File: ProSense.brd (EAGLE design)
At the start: 16.3 x 37.7 mm, 25 parts

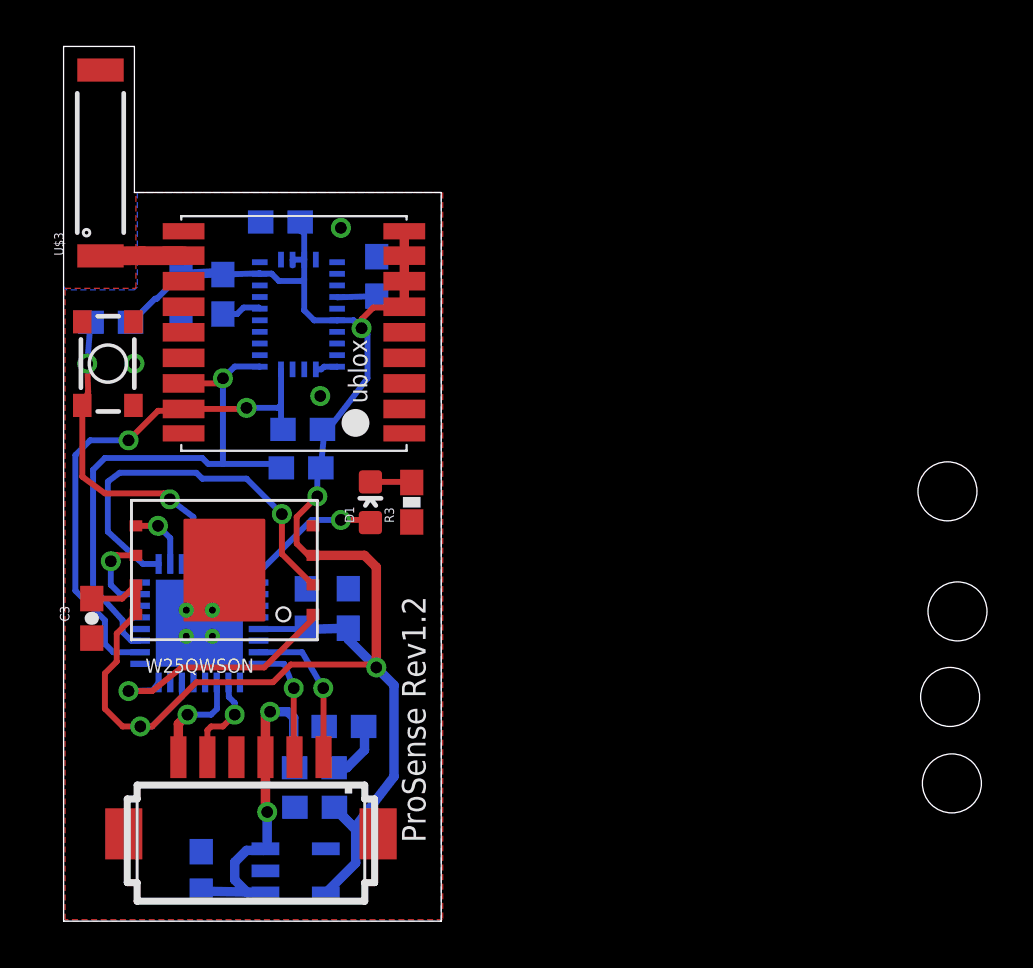
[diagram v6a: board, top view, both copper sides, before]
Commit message: Fixed up a few things. Need to fix ground pads and holes for qfn
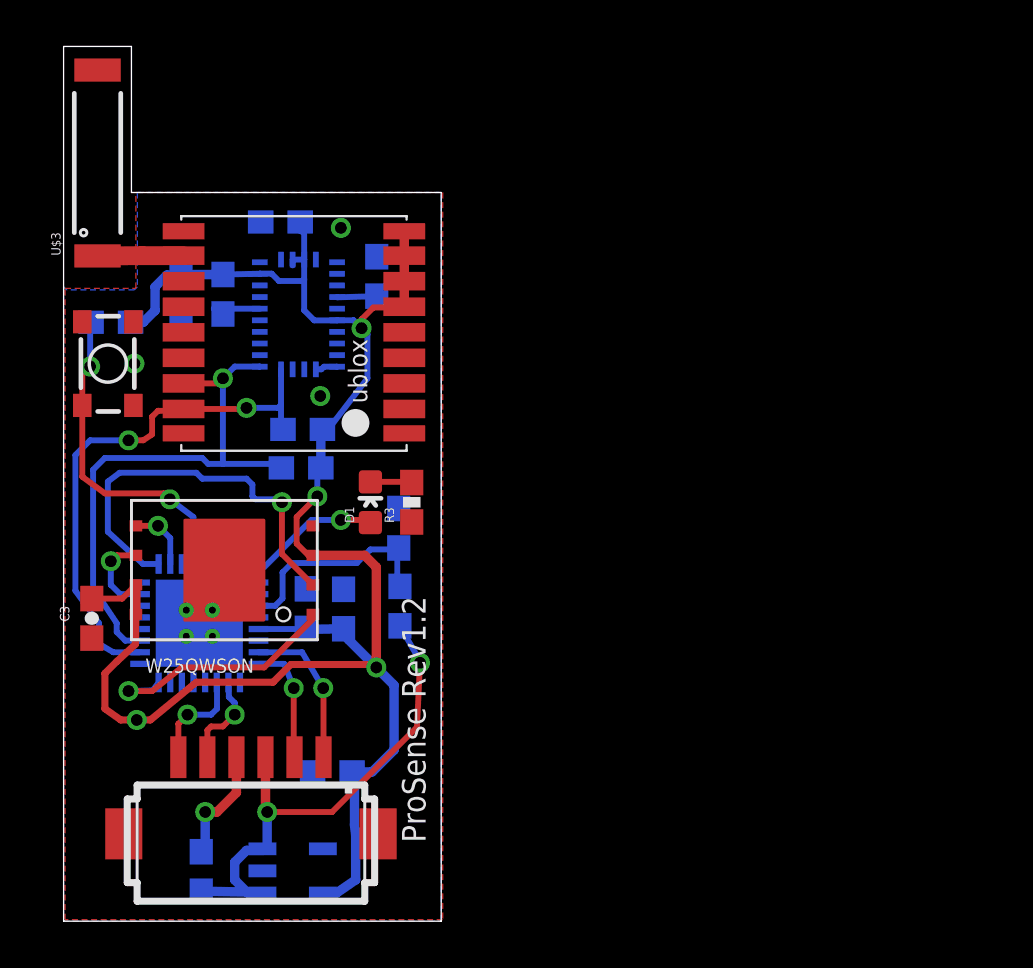
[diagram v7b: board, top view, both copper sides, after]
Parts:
- removed FRAME1: FRAME-LEDGER, SparkFun-Aesthetics:CREATIVE_COMMONS
- moved R2 8.86 mm to (20.0, 21.2), turned to 270 degrees
- moved R1 7.87 mm to (20.1, 17.9), turned to 270 degrees
- moved C15 1.70 mm to (17.2, 10.7)
- moved C7 0.20 mm to (17.6, 17.8)
- moved U$3 0.13 mm to (7.05, 37.0)
- moved MIC5205 0.13 mm to (15.4, 6.48)
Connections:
- net BAT_MONITOR: now also MCU.27; no longer MCU.24
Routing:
- net VIN: track 16.0 -> 23.3 mm
- net BAT_MONITOR: track 2.65 -> 9.36 mm
- net GND: track 2.69 -> 8.63 mm, vias 3 -> 4
- net VCC: track 84.4 -> 83.4 mm
- net WS_DO: track 16.8 -> 17.4 mm
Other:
- outline, holes or cut-outs redrawn

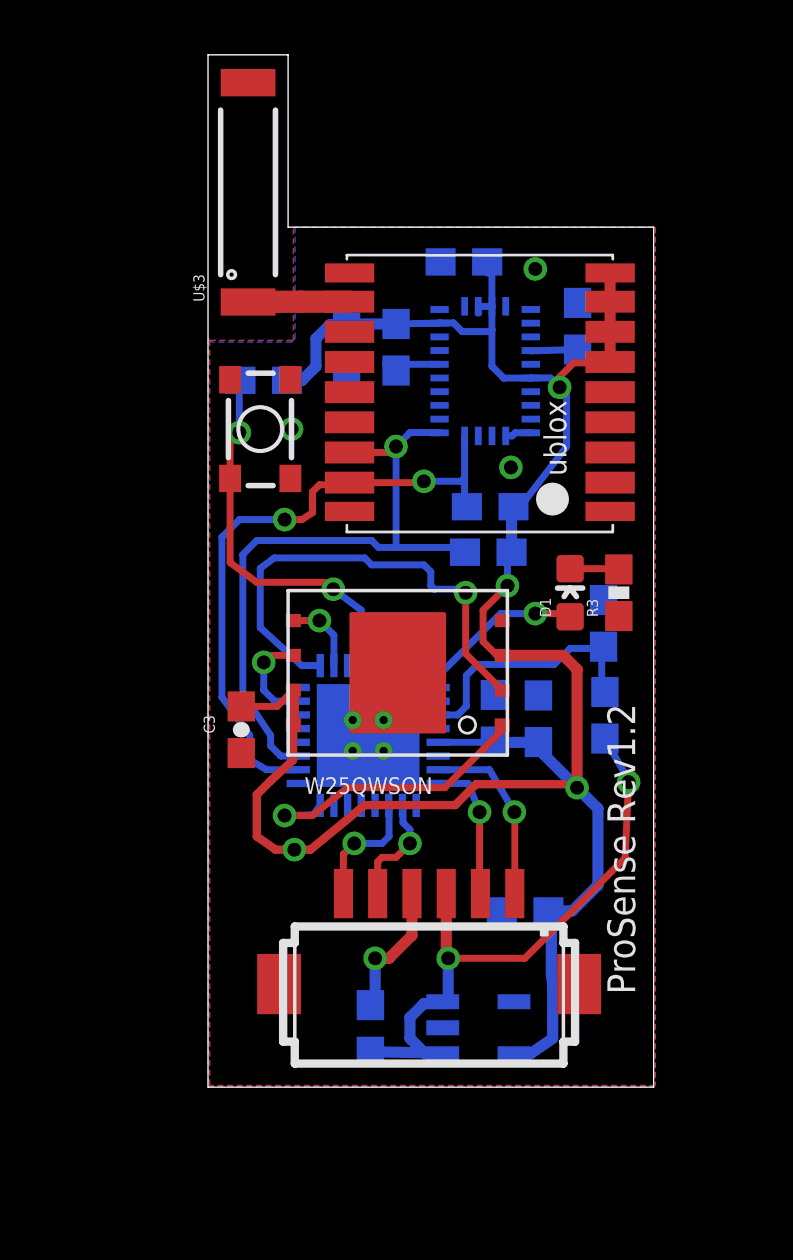
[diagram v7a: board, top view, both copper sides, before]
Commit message: MTK3339 readded
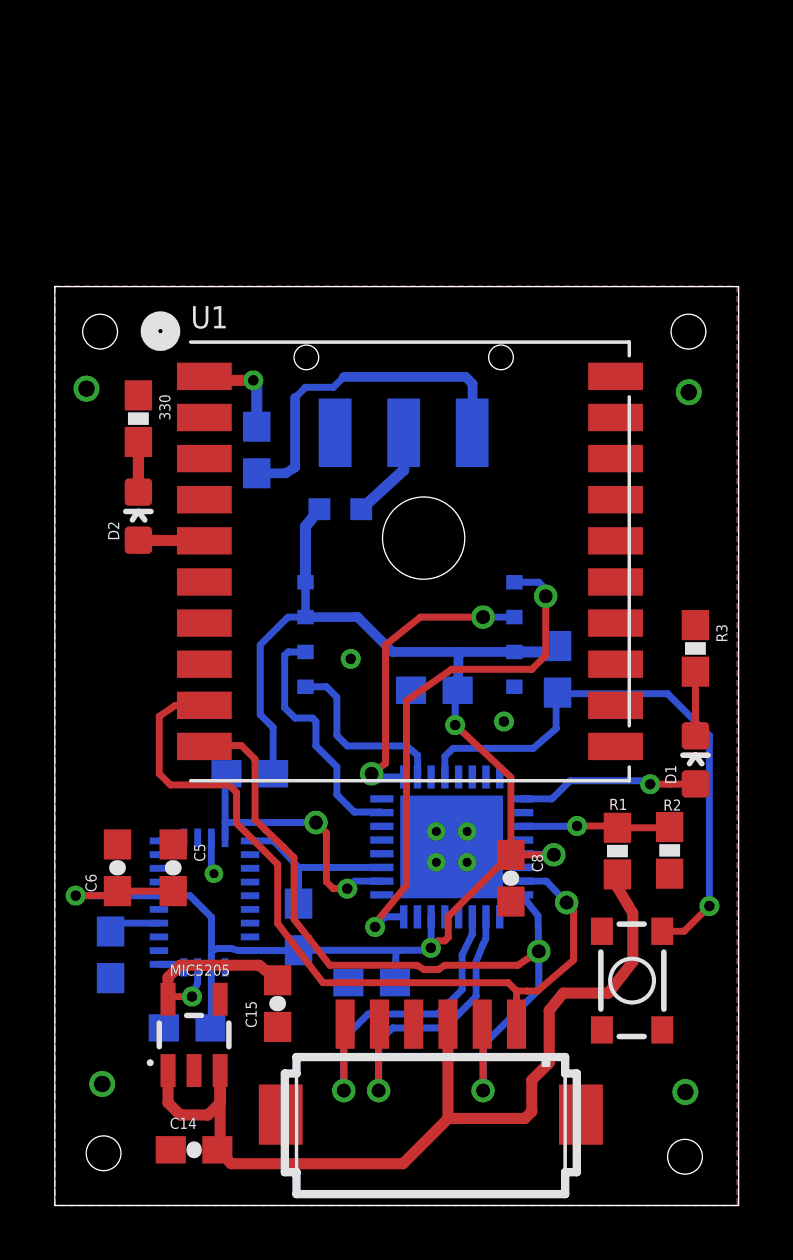
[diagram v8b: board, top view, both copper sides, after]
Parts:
- removed U$2: UBLOX_MAX, Ava:UBLOX_MAX
- removed U$3: ANTENNA2SMD3, SparkFun-RF:ANTENNA-CHIP4
- added 330: (no value), SparkFun-Passives:0603-RES
- added C4: 10uF, SparkFun-Passives:0603-CAP
- added D2: (no value), SparkFun-LED:LED-0603
- added FB1: (no value), microbuilder:_0603MP
- added S1: (no value), SparkFun-Electromechanical:SWITCH-SPDT-SMD
- added U1: (no value), adafruit:FGPMMOPA6H
- moved C2 28.6 mm to (2.03, 9.14), turned to 90 degrees
- moved C1 26.0 mm to (4.83, 6.48), turned to 180 degrees
- moved C6 25.5 mm to (2.29, 12.3), flipped to the top, turned to 90 degrees
- moved S2 24.3 mm to (21.1, 8.20), turned to 90 degrees
- moved BNO055 21.9 mm to (5.46, 11.0), turned to 180 degrees
- moved C5 20.0 mm to (4.32, 12.3), flipped to the top, turned to 270 degrees
- moved R8 15.3 mm to (8.89, 10.2), turned to 270 degrees
- moved R4 15.0 mm to (18.3, 19.6), turned to 90 degrees
- moved R7 13.1 mm to (7.11, 15.7)
- moved C7 11.4 mm to (11.6, 8.13), turned to 0 degrees
- moved MIC5205 10.4 mm to (5.08, 6.22), flipped to the top, turned to 0 degrees
- moved C15 9.64 mm to (8.13, 7.37), flipped to the top, turned to 90 degrees
- moved R2 8.62 mm to (22.4, 13.0), flipped to the top, turned to 90 degrees
- moved C14 7.81 mm to (5.08, 2.03), flipped to the top, turned to 0 degrees
- moved D1 7.62 mm to (23.4, 16.3)
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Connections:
- new net N$3: C4.1, S1.1
- new net N$4: D2.A, U1.P$5
- new net N$6: C4.2, U1.P$1
- new net N$7: FB1.1, S1.2
- net GND: now also 330.1, U1.P$12, U1.P$19, U1.P$3, U1.P$8; no longer U$2.10_GND, U$2.12_GND, U$2.1_GND
- net LPC_RX: now also U1.P$9
- net LPC_TX: now also U1.P$10
- net N$1: now also 330.2, D2.C; no longer U$2.11_RF_IN, U$3.SIG
- net SCL: no longer U$2.17_SCL2
- net SDA: no longer U$2.16_SDA2
- net VCC: now also FB1.2; no longer U$2.6_V_BCKP, U$2.7_VCC_IO, U$2.8_VCC, U$2.9_V_RESET
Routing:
- net LPC_TX: track 5.21 -> 30.3 mm, vias 1 -> 2
- net LPC_RX: track 6.65 -> 30.2 mm
- net SDA: track 24.3 -> 6.55 mm, vias 1 -> 0
- net VCC: track 83.4 -> 68.6 mm, vias 4 -> 5
- net SCL: track 23.1 -> 10.2 mm
- net N$3: track 0.00 -> 12.7 mm
- net VIN: track 23.3 -> 34.7 mm, vias 2 -> 0
- net WS_CS: track 10.8 -> 19.2 mm, vias 1 -> 2
- net ISP: track 4.51 -> 12.1 mm
- net RESET: track 4.12 -> 11.4 mm
- net BTN: track 14.2 -> 21.0 mm, vias 2 -> 1
- net WS_DO: track 17.4 -> 11.2 mm, vias 1 -> 2
- net GND: track 8.63 -> 3.27 mm, vias 4 -> 7
- net WS_SCK: track 3.63 -> 8.97 mm, vias 1 -> 0
- net BAT_MONITOR: track 9.36 -> 5.43 mm, vias 0 -> 1
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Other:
- board size 16.3 x 37.7 mm -> 24.9 x 33.5 mm
- board text removed: "ProSense Rev1.2"
